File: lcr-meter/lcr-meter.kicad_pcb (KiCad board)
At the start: 4 copper layers, 119 parts, among them J1 Conn_ARM_SWD_TagConnect_TC203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, J19 Barrel_Jack, J4 Conn_01x04, Q1 DMP3013SFV-7, SW1 SW_MEC_5E, SW2 SW_MEC_5E, U1 KC2016Z20.0000C15XXK, U10 AMP03GPZ, U11 TMUX1101DCK, U12 TMUX1101DCK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

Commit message: Component grouping started
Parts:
- removed C21: 100n, Capacitor_SMD:C_0402_1005Metric
- removed TP2: TestPoint, TestPoint:TestPoint_Pad_2.0x2.0mm
- added C36: 4.7u, Capacitor_SMD:C_0805_2012Metric, F.Cu at (79.0, 196.0)
- added C51: 4.7u, Capacitor_SMD:C_0805_2012Metric, F.Cu at (79.0, 171.3)
- C10, C11, C8, C9: footprint Capacitor_SMD:C_0402_1005Metric -> Capacitor_SMD:C_0805_2012Metric
- SW1, SW2: value SW_MEC_5E -> SW_Push
- moved Q1 154.7 mm to (32.5, 20.5), turned to 180 degrees
- moved D4 153.1 mm to (37.7, 20.7)
- moved C40 147.9 mm to (35.2, 19.7), turned to 90 degrees
- moved R26 143.8 mm to (36.7, 18.2)
- moved C9 143.7 mm to (88.5, -15.8), turned to 180 degrees
- moved C8 143.4 mm to (84.2, -15.8)
- moved C11 142.4 mm to (108.5, -16.0), turned to 180 degrees
- moved C10 141.4 mm to (104.2, -16.0)
- moved C42 140.6 mm to (42.2, 20.8), turned to -90 degrees
- moved R11 139.2 mm to (81.0, -21.8), turned to 90 degrees
- moved U7 136.1 mm to (106.0, -20.8)
- moved R12 135.7 mm to (81.0, -23.8), turned to 90 degrees
- moved J19 133.3 mm to (27.9, 21.0)
- moved U6 132.9 mm to (86.0, -20.5)
- moved C18 129.1 mm to (25.8, 47.3)
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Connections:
- SW1 pad 2: GND -> /MCU/Button 0
- SW2 pad 2: GND -> /MCU/Button 1
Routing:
- added copper zone on B.Cu, net GND
- added copper zone on F.Cu, net GND
- added copper zone on In1.Cu, net GND
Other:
- board outline added: 100 x 62 mm

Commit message: Component grouping completed
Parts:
- added H1: MountingHole_Pad, MountingHole:MountingHole_3.2mm_M3_Pad_Via, F.Cu at (83.0, 83.0)
- added H2: MountingHole_Pad, MountingHole:MountingHole_3.2mm_M3_Pad_Via, F.Cu at (193.0, 83.0)
- added H3: MountingHole_Pad, MountingHole:MountingHole_3.2mm_M3_Pad_Via, F.Cu at (83.0, 143.0)
- added H4: MountingHole_Pad, MountingHole:MountingHole_3.2mm_M3_Pad_Via, F.Cu at (193.0, 143.0)
- C35, C38: footprint Capacitor_SMD:C_0805_2012Metric -> Capacitor_SMD:C_0402_1005Metric
- U4: moved to B.Cu
- moved R23 156.3 mm to (113.2, 140.2), turned to -90 degrees
- moved R21 156.1 mm to (98.0, 140.2), turned to -90 degrees
- moved U6 155.7 mm to (102.8, 134.2), turned to -90 degrees
- moved U7 155.5 mm to (118.0, 134.2), turned to -90 degrees
- moved R12 155.0 mm to (106.0, 129.2), turned to 0 degrees
- moved R13 154.6 mm to (121.2, 129.2), turned to 0 degrees
- moved C11 152.8 mm to (113.2, 136.8), turned to 90 degrees
- moved C9 152.8 mm to (98.0, 136.8), turned to 90 degrees
- moved R11 152.7 mm to (104.0, 129.3), turned to 0 degrees
- moved R14 152.3 mm to (119.2, 129.2), turned to 0 degrees
- moved C8 148.9 mm to (98.0, 132.5), turned to -90 degrees
- moved C10 148.8 mm to (113.2, 132.5), turned to -90 degrees
- moved C33 136.0 mm to (167.0, 93.8)
- moved C43 136.0 mm to (167.0, 90.8)
- moved C44 136.0 mm to (167.0, 92.8)
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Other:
- board size 100 x 62 mm -> 120 x 70 mm
- board text added: "+1V8"
- board text added: "+3V3"
- board text added: "+5V"
- board text added: "-5V"
- board text added: "ADC"
- board text added: "Power Input"
- board text added: "STM32F446"
- board text added: "Sensing"
- board text added: "Sine Gen"

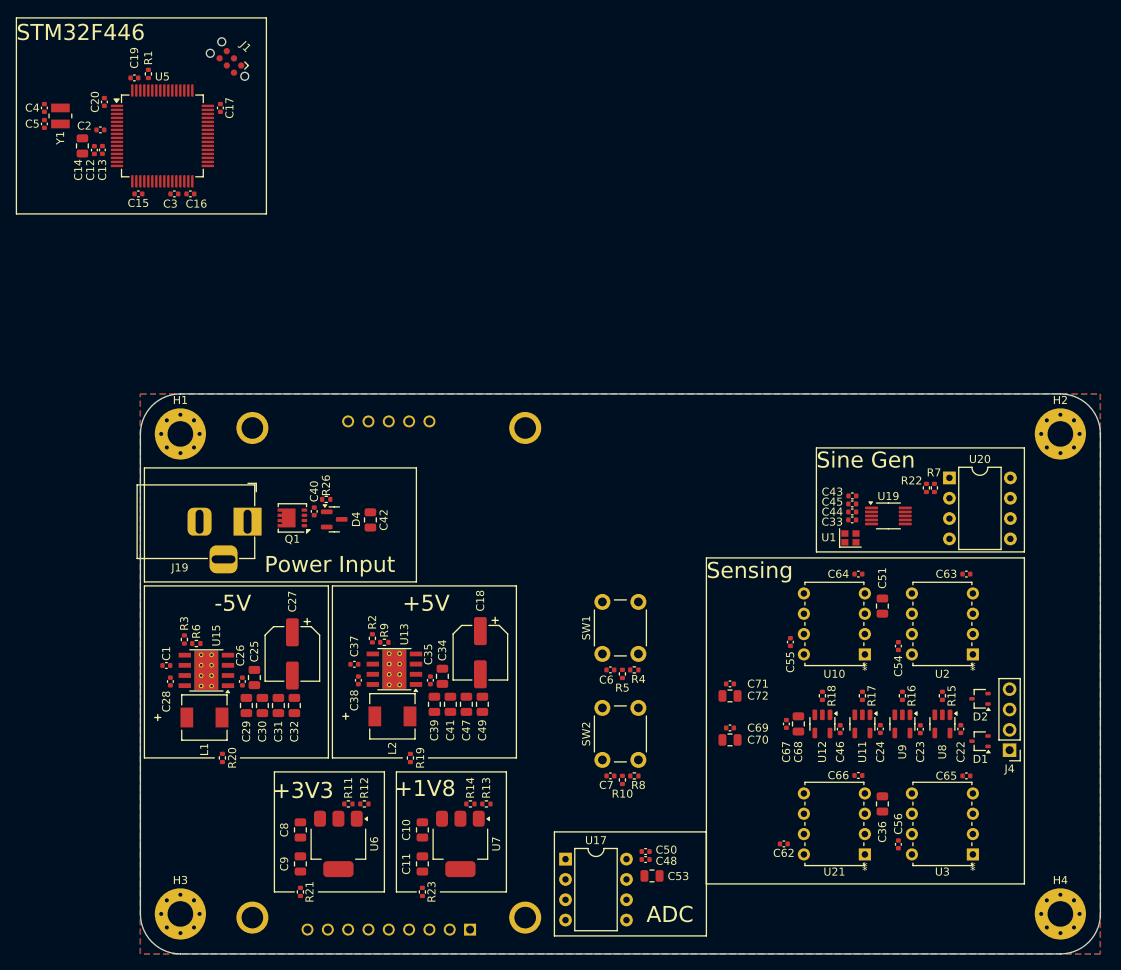
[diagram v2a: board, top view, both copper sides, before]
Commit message: Order submitteed, Mod board submitted
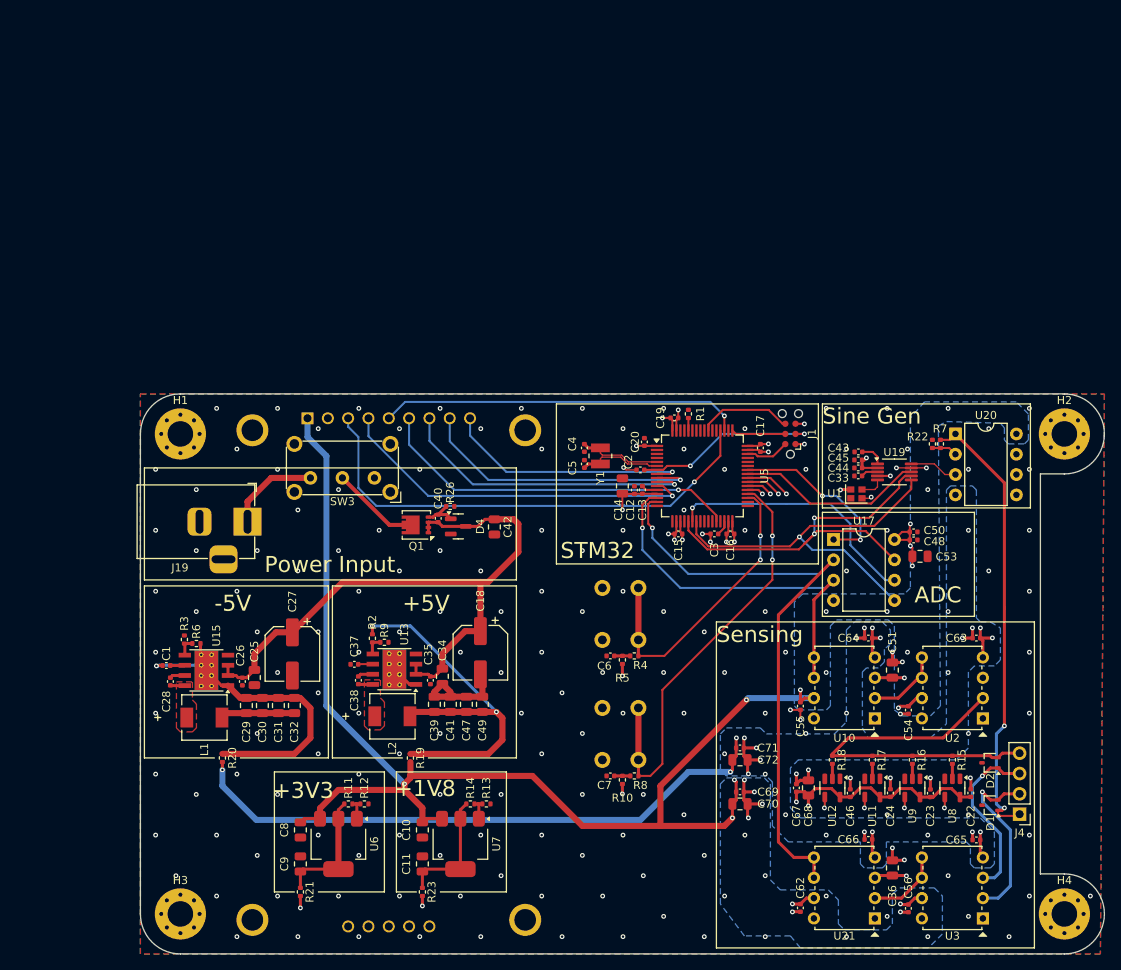
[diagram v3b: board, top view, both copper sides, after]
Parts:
- added SW3: SW_SPDT, Button_Switch_THT:SW_E-Switch_EG1224_SPDT_Angled, F.Cu at (107.2, 88.5)
- SW1, SW2: moved to B.Cu
- moved J1 84.0 mm to (159.2, 83.0), turned to 90 degrees
- moved C12 79.8 mm to (139.8, 90.0)
- moved C13 79.8 mm to (140.8, 90.0)
- moved C14 79.8 mm to (138.2, 89.5)
- moved C15 79.8 mm to (145.2, 95.5)
- moved C16 79.8 mm to (151.8, 95.5)
- moved C17 79.8 mm to (155.5, 84.8)
- moved C19 79.8 mm to (144.8, 81.0)
- moved C2 79.8 mm to (140.5, 87.5)
- moved C20 79.8 mm to (141.0, 84.0)
- moved C3 79.8 mm to (149.8, 95.5)
- moved C4 79.8 mm to (133.5, 84.8)
- moved C5 79.8 mm to (133.5, 86.8)
- moved R1 79.8 mm to (146.5, 80.5)
- moved U5 79.8 mm to (148.2, 88.2)
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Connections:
- J19 pad 1: Net-(Q1-D) -> Net-(SW3-C)
- U19 pad 2: +3.3V -> +3V3
- U5 pad 37: unconnected-(U5-PC6-Pad37) -> /MCU/Range_3
- U5 pad 38: unconnected-(U5-PC7-Pad38) -> /MCU/Range_2
- U5 pad 39: unconnected-(U5-PC8-Pad39) -> /MCU/Range_1
- U5 pad 40: unconnected-(U5-PC9-Pad40) -> /MCU/Range_0
- U5 pad 57: /MCU/Range_0 -> unconnected-(U5-PB5-Pad57)
- U5 pad 58: /MCU/Range_1 -> unconnected-(U5-PB6-Pad58)
- U5 pad 59: /MCU/Range_2 -> unconnected-(U5-PB7-Pad59)
- U5 pad 61: /MCU/Range_3 -> unconnected-(U5-PB8-Pad61)
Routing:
- net +5V: track 0.00 -> 167.6 mm, vias 0 -> 8
- net +1V8: track 0.00 -> 100.6 mm, vias 0 -> 3
- net GND: track 0.00 -> 94.5 mm, vias 0 -> 207
- net -5V: track 0.00 -> 92.2 mm, vias 0 -> 9
- net +12V: track 0.00 -> 81.3 mm
- net /ADC/CH0: track 0.00 -> 76.8 mm, vias 0 -> 1
- net /MCU/Range_1: track 0.00 -> 67.9 mm, vias 0 -> 2
- net +3V3: track 0.00 -> 67.4 mm, vias 0 -> 17
- net /MCU/Range_3: track 0.00 -> 67.3 mm, vias 0 -> 2
- net /MCU/Range_2: track 0.00 -> 67.3 mm, vias 0 -> 2
- net /MCU/Range_0: track 0.00 -> 66.4 mm, vias 0 -> 2
- net /LCD/NCS: track 0.00 -> 61.2 mm, vias 0 -> 1
- net /Sensing/I_Out: track 0.00 -> 56.9 mm, vias 0 -> 2
- net /MCU/Button 1: track 0.00 -> 53.3 mm, vias 0 -> 2
- net /ADC/ADC_CLK: track 0.00 -> 48.8 mm, vias 0 -> 2
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- added copper zone on In2.Cu, net +3V3
- added copper zone on B.Cu, net +5V
- added copper zone on B.Cu, net -5V
- added copper zone on F.Cu, net Net-(U13-SW)
- added copper zone on F.Cu, net Net-(U15-SW)
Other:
- board size 120 x 70 mm -> 120.5 x 70 mm
- board text added: "Current In"
- board text added: "Current Out"
- board text added: "Precision LCR Meter Rev A Jacob Lundstrom NDSU Fall 2024"
- board text added: "STM32"
- board text added: "Sense V+"
- board text added: "Sense V-"
- board text added: "jacob.lundstrom.EE@gmail.com"
- board text removed: "STM32F446"

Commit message: Rev A schematic fixes
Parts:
- added U14: LF353N/NOPB, Package_DIP:DIP-8_W7.62mm, F.Cu at (202.2, 135.7)
- added U16: LF353N/NOPB, Package_DIP:DIP-8_W7.62mm, F.Cu at (192.4, 111.0)
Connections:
- net /Sensing/I_Out renamed /DAC/I_OUT
- C6 pad 1: Net-(C6-Pad1) -> /MCU/Button 0
- C7 pad 1: Net-(C7-Pad1) -> /MCU/Button 1
- D1 pad 2: /Sensing/V_Sense+ -> Net-(J4-Pin_2)
- D2 pad 1: /Sensing/V_Sense- -> Net-(J4-Pin_3)
- J4 pad 2: /Sensing/V_Sense+ -> Net-(J4-Pin_2)
- J4 pad 3: /Sensing/V_Sense- -> Net-(J4-Pin_3)
- R10 pad 1: Net-(C7-Pad1) -> /MCU/Button 1
- R4 pad 1: /MCU/Button 0 -> Net-(R4-Pad1)
- R4 pad 2: Net-(C6-Pad1) -> /MCU/Button 0
- R5 pad 1: Net-(C6-Pad1) -> /MCU/Button 0
- R8 pad 1: /MCU/Button 1 -> Net-(R8-Pad1)
- R8 pad 2: Net-(C7-Pad1) -> /MCU/Button 1
- SW1 pad 2: /MCU/Button 0 -> Net-(R4-Pad1)
- SW2 pad 2: /MCU/Button 1 -> Net-(R8-Pad1)
- U2 pad 2: /Sensing/I_In -> /Sensing/BUF_Shunt+
- U2 pad 3: GND -> /Sensing/BUF_Shunt-
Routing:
- net Net-(R8-Pad1): track 0.00 -> 8.50 mm
- net Net-(R4-Pad1): track 0.00 -> 8.50 mm
- net /MCU/Button 0: track 37.6 -> 33.7 mm
- net /MCU/Button 1: track 53.3 -> 49.6 mm
- net Net-(C7-Pad1): track 2.02 -> 0.00 mm
- net Net-(C6-Pad1): track 2.01 -> 0.00 mm
- net GND: vias 207 -> 182

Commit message: PCB updates
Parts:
- removed J19: Barrel_Jack, Connector_BarrelJack:BarrelJack_Horizontal
- removed R19, R20, R21, R23: 0R, Resistor_SMD:R_0402_1005Metric
- removed U7: LM1117MP-ADJ, Package_TO_SOT_SMD:SOT-223-3_TabPin2
- added C21: 100n, Capacitor_SMD:C_0402_1005Metric, F.Cu at (183.6, 133.2)
- added C52: 10n, Capacitor_SMD:C_0402_1005Metric, F.Cu at (178.3, 84.2)
- added C57: 100n, Capacitor_SMD:C_0402_1005Metric, F.Cu at (175.4, 117.0)
- added C58: 100n, Capacitor_SMD:C_0402_1005Metric, F.Cu at (184.0, 108.0)
- added J2: Conn_01x02, Connector_PinHeader_2.54mm:PinHeader_1x02_P2.54mm_Vertical, F.Cu at (82.8, 94.3)
- added JP1: Jumper_2_Open, Jumper:SolderJumper-2_P1.3mm_Open_TrianglePad1.0x1.5mm, F.Cu at (112.1, 123.6)
- added JP2: Jumper_2_Open, Jumper:SolderJumper-2_P1.3mm_Open_TrianglePad1.0x1.5mm, F.Cu at (88.4, 123.7)
- added JP3: Jumper_2_Open, Jumper:SolderJumper-2_P1.3mm_Open_TrianglePad1.0x1.5mm, F.Cu at (98.6, 140.3)
- added JP4: Jumper_2_Open, Jumper:SolderJumper-2_P1.3mm_Open_TrianglePad1.0x1.5mm, F.Cu at (113.8, 140.3)
- C10: value 10u -> 20p; footprint Capacitor_SMD:C_0805_2012Metric -> Capacitor_SMD:C_0402_1005Metric
- C11: value 10u -> 100n; footprint Capacitor_SMD:C_0805_2012Metric -> Capacitor_SMD:C_0402_1005Metric
- R13: value 500R -> 12k
- R14: value 1k -> 12k
- R26: value 12K 1% -> 12k
- U11, U12, U8, U9: footprint Package_TO_SOT_SMD:SOT-23-5 -> Package_TO_SOT_SMD:SOT-353_SC-70-5
- moved C10 77.4 mm to (176.0, 87.2)
- moved C11 62.4 mm to (175.4, 141.8)
- moved U14 18.9 mm to (184.8, 143.1), turned to 180 degrees
- moved C36 12.1 mm to (159.9, 136.8)
- moved C51 12.1 mm to (159.9, 112.0)
- moved C54 12.1 mm to (161.9, 117.0)
- moved C55 12.1 mm to (148.4, 116.5)
- moved C56 12.1 mm to (161.9, 141.8)
- moved C62 12.1 mm to (148.4, 141.8)
- moved C63 12.1 mm to (170.4, 108.0)
- moved C64 12.1 mm to (156.9, 108.0)
- moved C65 12.1 mm to (170.4, 133.2)
- moved C66 12.1 mm to (156.9, 133.2)
- moved U10 12.1 mm to (157.8, 118.1)
- moved U2 12.1 mm to (171.3, 118.1)
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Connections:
- C10 pad 1: +5V -> /DAC/Signal
- C11 pad 1: Net-(U7-VO) -> +5V
- C9 pad 1: Net-(U6-VO) -> Net-(JP3-A)
- R11 pad 1: Net-(U6-VO) -> Net-(JP3-A)
- R13 pad 1: Net-(U7-ADJ) -> Net-(JP3-A)
- R13 pad 2: GND -> Net-(JP4-A)
- R14 pad 1: Net-(U7-VO) -> Net-(JP4-A)
- R14 pad 2: Net-(U7-ADJ) -> GND
- U5 pad 10: /LCD/SCK -> /LCD/DC
- U5 pad 11: /LCD/RESET -> /LCD/LED
- U5 pad 51: /LCD/DC -> /LCD/SCK
- U5 pad 52: /LCD/NCS -> /LCD/MISO
- U5 pad 8: /LCD/MISO -> /LCD/NCS
- U5 pad 9: /LCD/LED -> /LCD/RESET
- U6 pad 2: Net-(U6-VO) -> Net-(JP3-A)
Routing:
- net +5V: track 167.6 -> 133.3 mm, vias 8 -> 39
- net GND: track 94.5 -> 121.9 mm, vias 182 -> 106
- net Net-(JP3-A): track 0.00 -> 26.5 mm
- net +1V8: track 100.6 -> 78.6 mm, vias 3 -> 0
- net Net-(J4-Pin_3): track 0.00 -> 18.4 mm, vias 0 -> 1
- net /Sensing/BUF_Shunt+: track 0.00 -> 18.1 mm
- net Net-(J4-Pin_2): track 0.00 -> 17.9 mm, vias 0 -> 1
- net Net-(U7-VO): track 15.4 -> 0.00 mm
- net Net-(U6-VO): track 15.4 -> 0.00 mm
- net /Sensing/V_Sense-: track 21.8 -> 8.41 mm, vias 1 -> 0
- net Net-(JP4-A): track 0.00 -> 12.1 mm
- net Net-(Q1-D): track 11.2 -> 21.5 mm
- net /Sensing/I_In: track 45.7 -> 55.4 mm
- net /Sensing/BUF_Shunt-: track 0.00 -> 8.41 mm
- net /ADC/CH1: track 47.3 -> 54.9 mm
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- added copper zone on F.Cu, net +5V
- removed copper zone on B.Cu, net -5V
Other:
- board text added: "Jacob.Lundstrom.EE@gmail.com"
- board text added: "Precision LCR Meter [Rev B] Jacob Lundstrom NDSU Fall 2024"
- board text removed: "Precision LCR Meter Rev A Jacob Lundstrom NDSU Fall 2024"
- board text removed: "jacob.lundstrom.EE@gmail.com"

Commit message: Rev B Fixes
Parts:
- added C59: 100n, Capacitor_SMD:C_0402_1005Metric, F.Cu at (175.4, 141.8)
- added C60: 100n, Capacitor_SMD:C_0402_1005Metric, F.Cu at (183.8, 133.2)
- added J3: Conn_01x02, footprints:1-1337445-0, B.Cu at (207.5, 141.5)
- added J5: Conn_01x02, footprints:1-1337445-0, B.Cu at (207.5, 103.5)
- added J6: Conn_01x02, footprints:1-1337445-0, B.Cu at (207.5, 84.5)
- added J7: Conn_01x04, Connector_PinHeader_2.54mm:PinHeader_1x04_P2.54mm_Vertical, F.Cu at (188.2, 130.5)
- J4: value Conn_01x04 -> Conn_01x02; footprint Connector_PinHeader_2.54mm:PinHeader_1x04_P2.54mm_Vertical -> footprints:1-1337445-0; moved to B.Cu
- moved C11 62.1 mm to (186.5, 80.8), turned to 180 degrees
- moved C21 43.8 mm to (178.2, 89.8), turned to 90 degrees
- moved J4 21.2 mm to (207.5, 122.5), turned to 0 degrees
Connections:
- D1 pad 2: Net-(J4-Pin_2) -> /Sensing/BNCs/2
- D2 pad 1: Net-(J4-Pin_3) -> /Sensing/BNCs/3
- J4 pad 1: /DAC/I_OUT -> /Sensing/BNCs/2
- J4 pad 2: Net-(J4-Pin_2) -> GND
- U14 pad 3: Net-(J4-Pin_2) -> /Sensing/BNCs/2
- U14 pad 5: Net-(J4-Pin_3) -> /Sensing/BNCs/3
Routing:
- net /Sensing/BNCs/3: track 0.00 -> 54.1 mm
- net /Sensing/I_In: track 55.4 -> 107.9 mm
- net /Sensing/BNCs/2: track 0.00 -> 36.2 mm
- net /DAC/I_OUT: track 58.7 -> 85.7 mm, vias 2 -> 1
- net Net-(J4-Pin_3): track 18.4 -> 0.00 mm, vias 1 -> 0
- net Net-(J4-Pin_2): track 17.9 -> 0.00 mm, vias 1 -> 0
- net -5V: track 95.5 -> 101.8 mm, vias 11 -> 25
- net GND: track 121.9 -> 128.1 mm, vias 106 -> 304
- net +3V3: track 66.0 -> 70.2 mm, vias 17 -> 23
- net +5V: track 133.3 -> 135.8 mm
- net /Sensing/BUF_Shunt+: track 18.1 -> 17.1 mm
- added copper zone on B.Cu, net -5V
- added copper zone on F.Cu, net -5V
- added copper zone on In2.Cu, net GND
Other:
- board size 120.5 x 70 mm -> 137.5 x 70 mm

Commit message: REV B order submitted
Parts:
- removed C48: 100n, Capacitor_SMD:C_0402_1005Metric
- removed C50: 1u, Capacitor_SMD:C_0402_1005Metric
- removed C53: 4.7u, Capacitor_SMD:C_0805_2012Metric
- removed U17: MCP3202, Package_DIP:DIP-8_W7.62mm
- moved SW3 13.5 mm to (85.1, 90.3), turned to -90 degrees
- moved J2 10.9 mm to (93.5, 92.0)
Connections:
- net /ADC/ADC_CLK renamed /DAC/DAC_SCK
- net /ADC/ADC_DIN renamed /DAC/DAC_SDI
- net /ADC/CH0 renamed /MCU/STM32_ADC2_IN1
- net /ADC/CH1 renamed /MCU/STM32_ADC1_IN0
- U5 pad 22: /ADC/ADC_DOUT -> /MCU/SPI1_MISO
- U5 pad 42: /ADC/ADC_nCS -> unconnected-(U5-PA9-Pad42)
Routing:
- net /ADC/ADC_DOUT: track 33.5 -> 0.00 mm, vias 1 -> 0
- net /MCU/STM32_ADC2_IN1: track 82.8 -> 52.5 mm, vias 1 -> 0
- net /MCU/STM32_ADC1_IN0: track 54.9 -> 27.2 mm, vias 1 -> 0
- net /ADC/ADC_nCS: track 22.5 -> 0.00 mm, vias 2 -> 0
- net /DAC/DAC_SDI: track 48.4 -> 33.4 mm, vias 1 -> 0
- net /DAC/DAC_SCK: track 48.8 -> 37.9 mm
- net Net-(Q1-D): track 21.5 -> 32.2 mm
- net +3V3: track 70.2 -> 60.8 mm, vias 23 -> 20
- net GND: track 128.1 -> 137.1 mm, vias 304 -> 336
- net /DAC/DAC_nCS: track 23.6 -> 24.8 mm
- net /MCU/Range_3: track 66.9 -> 66.3 mm
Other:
- board text added: "+1V65"
- board text removed: "+1V8"
- board text removed: "ADC"
